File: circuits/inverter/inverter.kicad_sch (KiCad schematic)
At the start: 0 parts

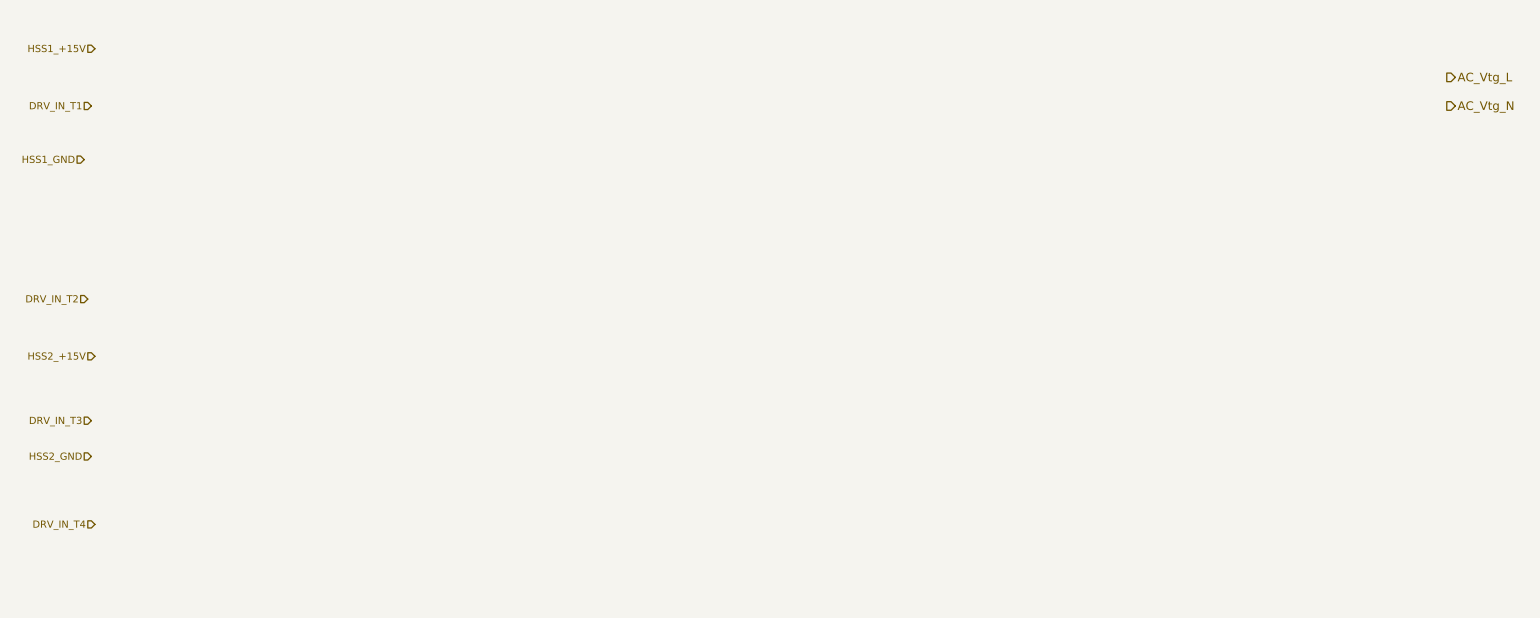
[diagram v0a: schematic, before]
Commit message: converts libraries to Kicad 6 format, updates bridge driver
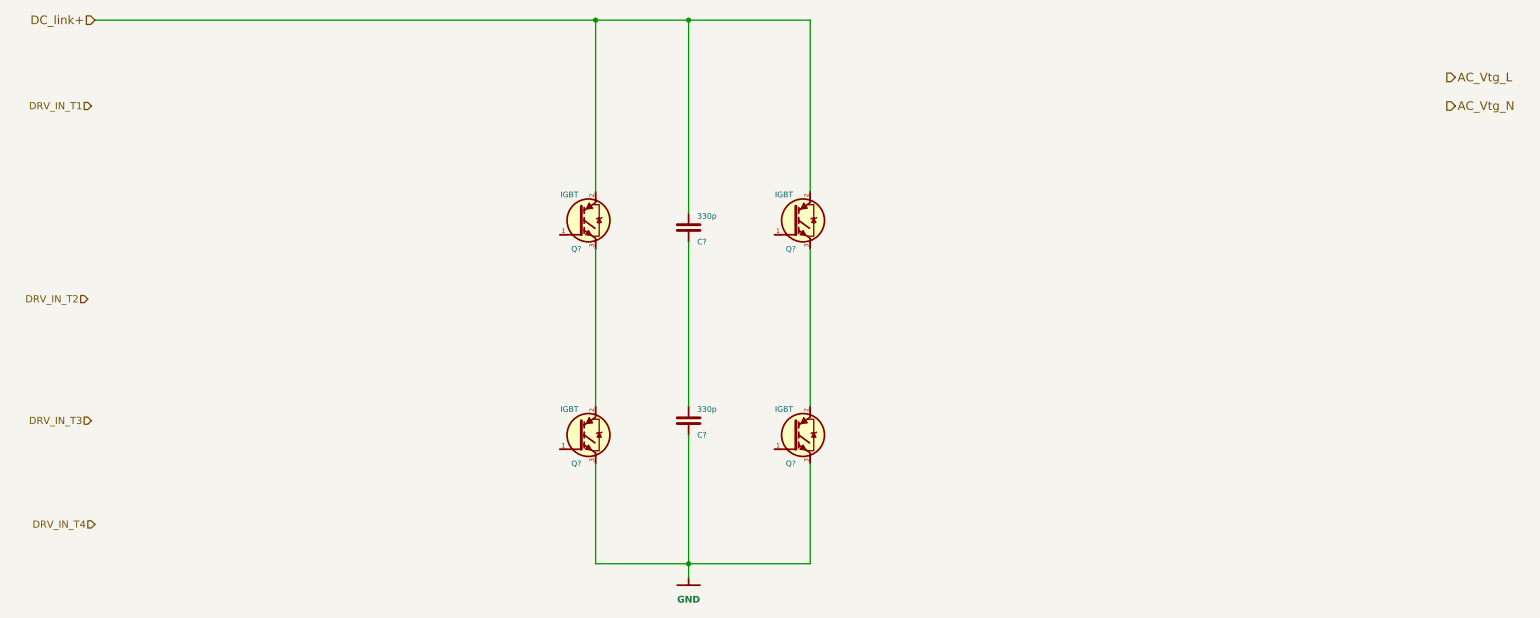
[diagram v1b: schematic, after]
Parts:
- added C? (x2): 330p, symbol OSSI_standard_components:Capacitor
- added Q? (x4): IGBT, symbol OSSI_standard_components:IGBT
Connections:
- new net: Q?.2 (C), Q?.3 (E) (x2)
- new net: C?.1, C?.2
- new net DC_link+: C?.2, Q?.2 (C), Q?.2 (C)
- new net GND: C?.1, Q?.3 (E), Q?.3 (E)

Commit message: updates circuits, adds linear regulator NCP1117
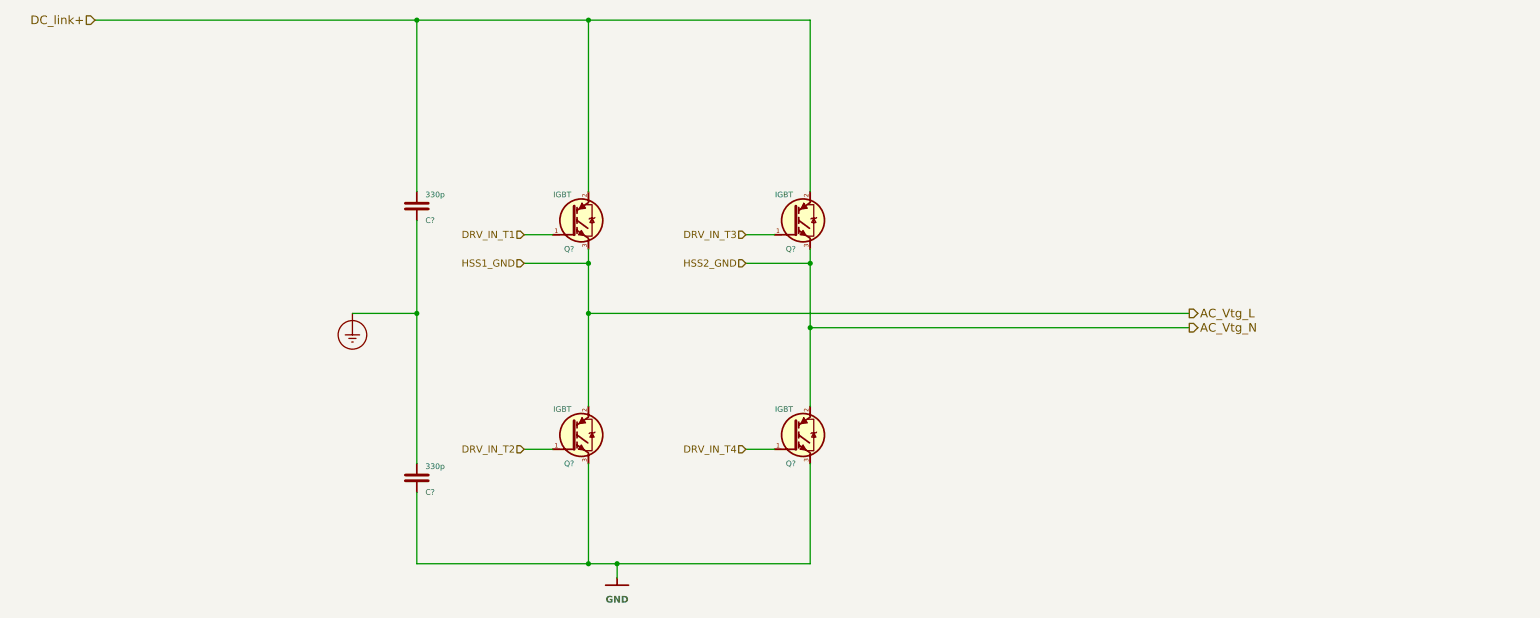
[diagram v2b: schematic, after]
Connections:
- net AC_Vtg_L: now also Q?.2 (C), Q?.3 (E)
- net AC_Vtg_N: now also Q?.2 (C), Q?.3 (E)
- net DRV_IN_T1: now also Q?.1 (G)
- net DRV_IN_T2: now also Q?.1 (G)
- net DRV_IN_T3: now also Q?.1 (G)
- net DRV_IN_T4: now also Q?.1 (G)
- net Earth_Protective: now reaches C?.1, C?.2
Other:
- moved on the sheet: C?, Q?
